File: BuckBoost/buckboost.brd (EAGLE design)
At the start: 100 x 80 mm, 8 parts

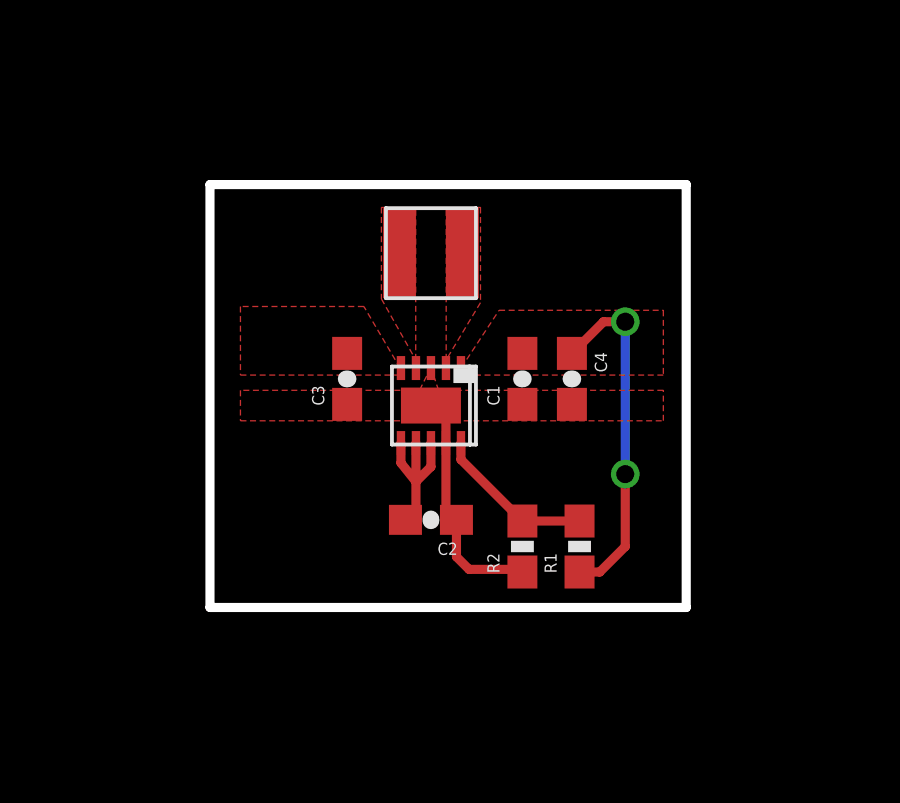
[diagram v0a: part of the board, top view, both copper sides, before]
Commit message: Changed Resistor and Capacity sizes
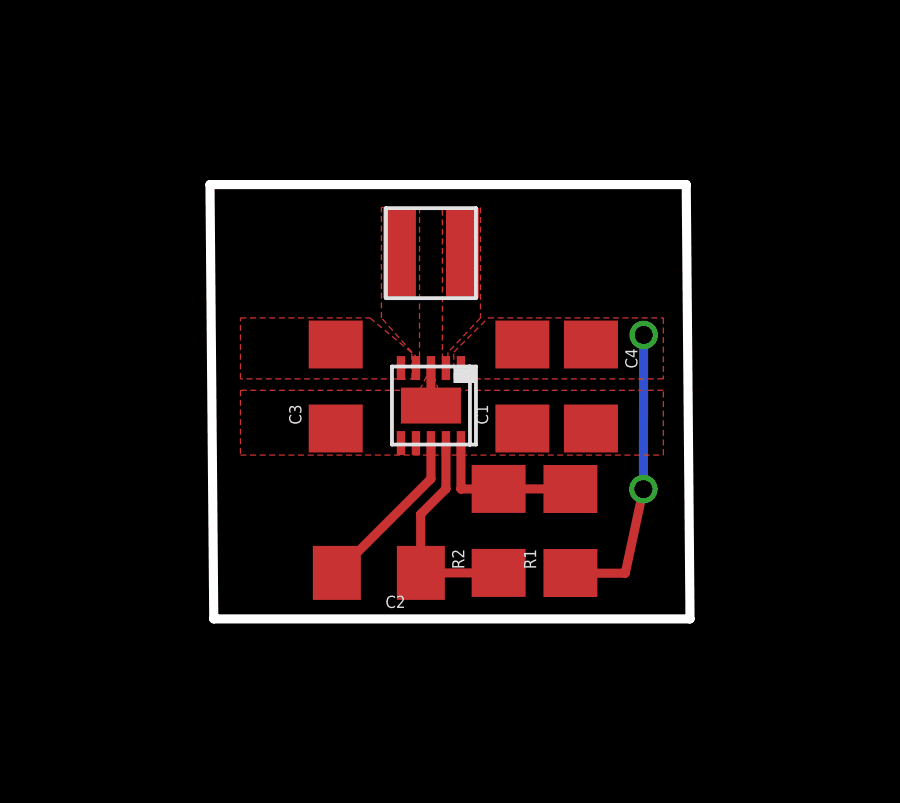
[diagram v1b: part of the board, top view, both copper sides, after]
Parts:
- C1, C2, C3, C4: device SparkFun-Passives:0603-CAP -> SparkFun-Capacitors:1206
- R1, R2: device SparkFun-Resistors:0603-RES -> SparkFun-Resistors:1206
- moved C2 2.48 mm to (13.5, 12.2)
- moved R2 0.95 mm to (17.5, 13.6)
- moved C4 0.68 mm to (20.6, 18.4)
- moved R1 0.60 mm to (19.9, 13.6)
- moved C3 0.46 mm to (12.1, 18.4)
- moved C1 0.25 mm to (18.3, 18.4)
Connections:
- new net N$2: U$1.6
- net N$3: no longer U$1.6, U$1.7
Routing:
- net VOUT: track 11.6 -> 9.84 mm
- net GND: track 7.80 -> 8.53 mm
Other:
- outline, holes or cut-outs redrawn

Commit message: PCB finished, only need to fix labels
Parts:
- added J1: (no value), SparkFun-Connectors:1X04
- added J2: (no value), SparkFun-Connectors:1X05
- added SJ1, SJ2: SOLDERJUMPERNC, SparkFun-Retired:SJ_2S
- moved R2 0.18 mm to (17.6, 13.5)
- moved R1 0.18 mm to (20.0, 13.5)
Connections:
- new net N$4: SJ2.2, U$1.7
- net GND: now also J2.2, J2.3, SJ2.1
- net N$2: now also SJ1.2
- net VIN: now also J2.1, J2.4, J2.5, SJ1.1
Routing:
- net N$2: track 0.00 -> 11.3 mm, vias 0 -> 2
- net N$4: track 0.00 -> 5.16 mm
- net VOUT: track 9.84 -> 10.4 mm
- added copper zone on layer 16, net GND
- added copper zone on layer 16, net VIN
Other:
- board size 100 x 80 mm -> 100.1 x 80.4 mm

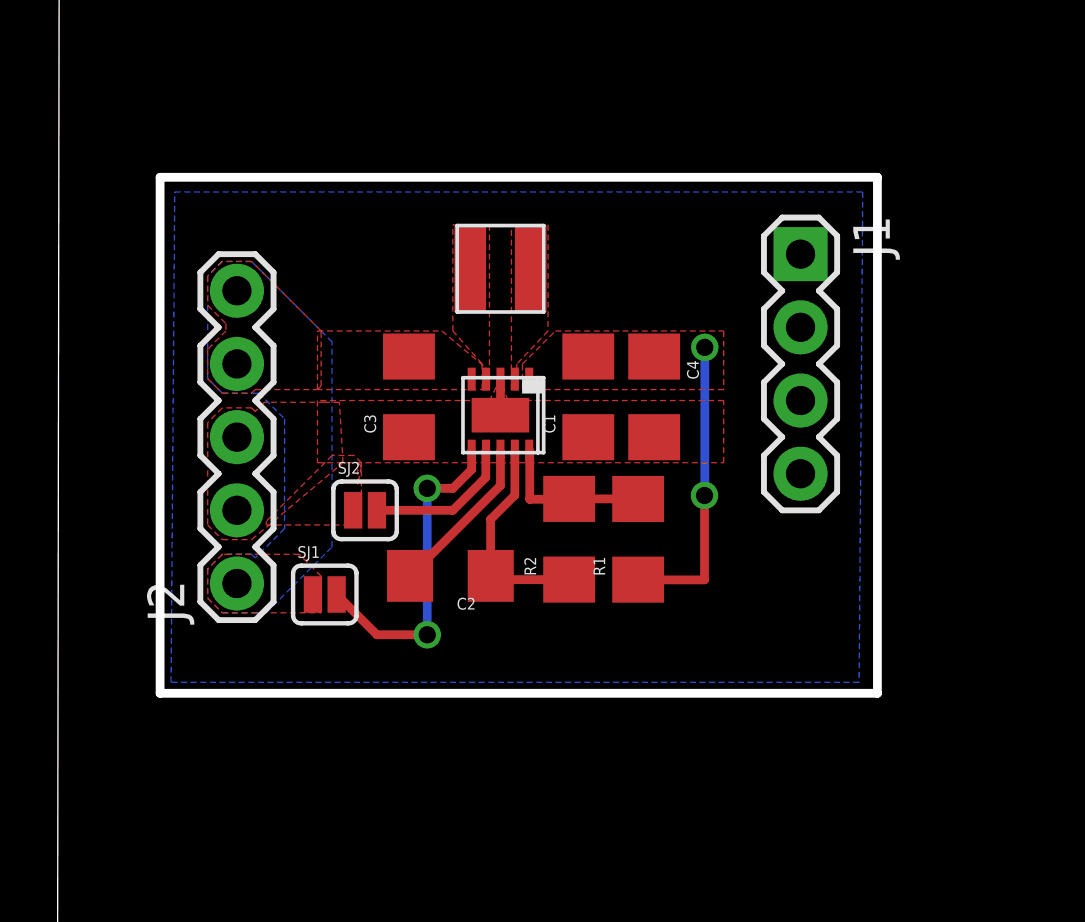
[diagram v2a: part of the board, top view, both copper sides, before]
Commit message: Headers Aligned for breadBoard
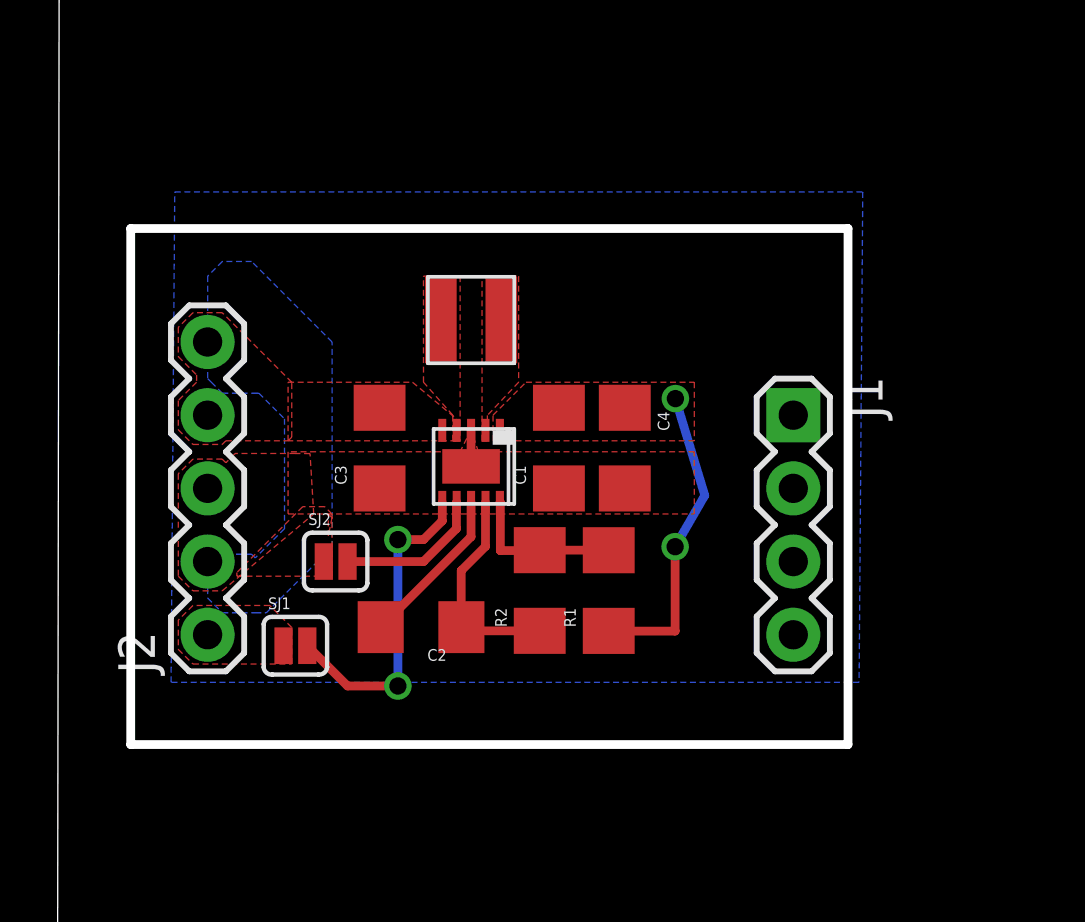
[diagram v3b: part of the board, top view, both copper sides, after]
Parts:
- moved J1 5.59 mm to (25.4, 17.8)
- moved U$1 2.05 mm to (14.2, 16.0)
- moved C2 2.05 mm to (12.5, 10.4)
- moved J2 2.05 mm to (5.08, 10.2)
- moved SJ1 2.05 mm to (8.12, 9.78)
- moved SJ2 2.05 mm to (9.52, 12.7)
- moved C1 2.05 mm to (17.3, 16.6)
- moved C3 2.05 mm to (11.0, 16.6)
- moved C4 2.05 mm to (19.6, 16.6)
- moved L1 2.05 mm to (14.2, 21.1)
- moved R1 2.05 mm to (19.0, 11.7)
- moved R2 2.05 mm to (16.6, 11.7)
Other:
- outline, holes or cut-outs redrawn

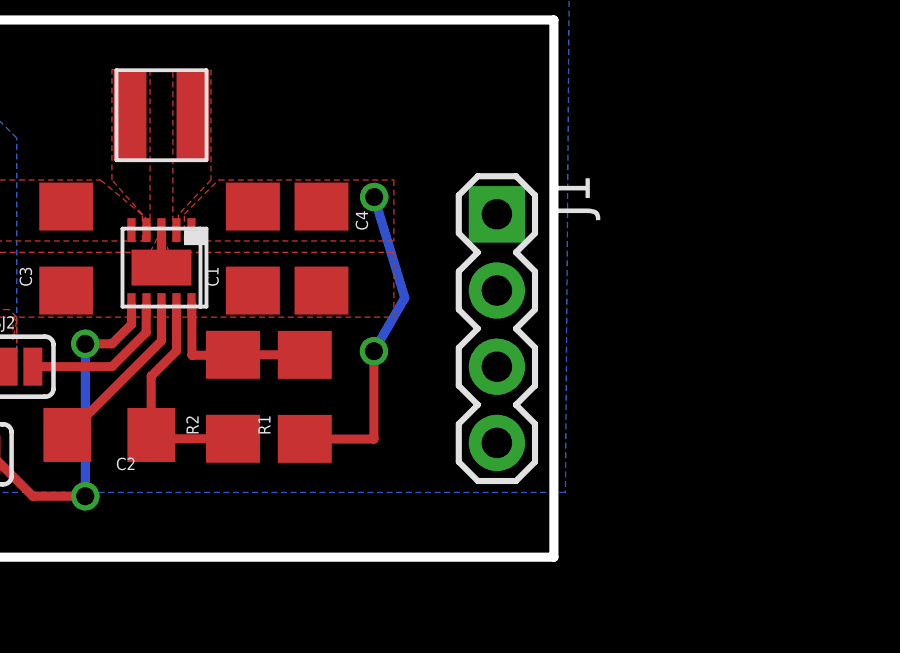
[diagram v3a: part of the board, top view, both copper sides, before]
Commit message: Finshed VOUT, just labels
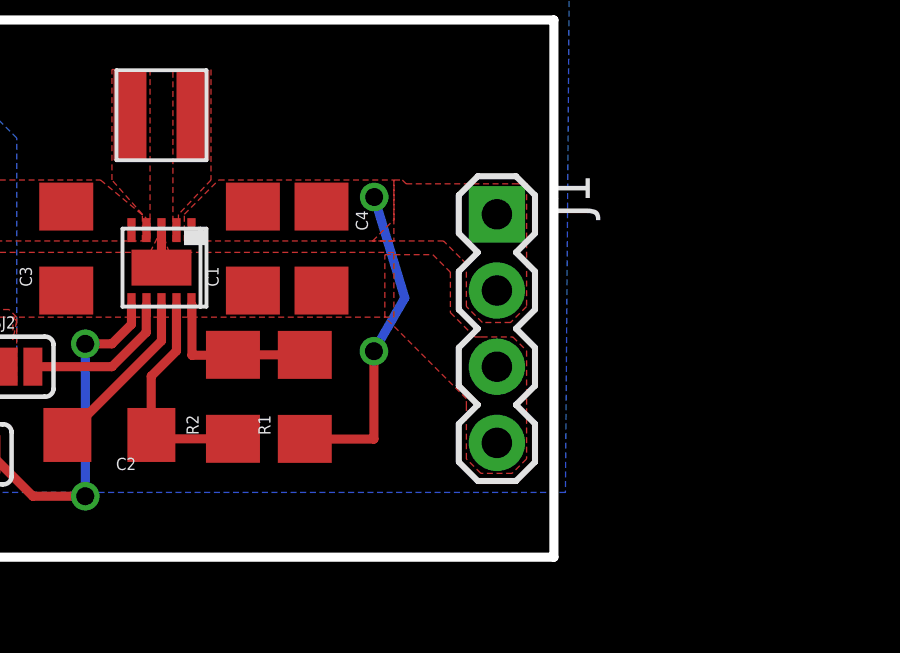
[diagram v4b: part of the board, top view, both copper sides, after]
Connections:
- net GND: now also J1.3, J1.4
- net VOUT: now also J1.1, J1.2
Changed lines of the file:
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@@
 <setting verticaltext="up"/>
 </settings>
-<grid distance="2.54" unitdist="mm" unit="mm" style="lines" multiple="1" display="yes" altdistance="0.000000123031" altunitdist="inch" altunit="inch"/>
+<grid distance="0.0254" unitdist="mm" unit="mm" style="lines" multiple="1" display="yes" altdistance="0.00254" altunitdist="mm" altunit="mm"/>
 <layers>
 <layer number="1" name="Top" color="4" fill="1" visible="yes" active="yes"/>
@@
 <wire x1="21.30178125" y1="13.21575" x2="22.3308" y2="14.99375" width="0.3048" layer="16"/>
 <wire x1="22.3308" y1="14.99375" x2="21.31115625" y2="18.354959375" width="0.3048" layer="16"/>
+<polygon width="0.3048" layer="1" thermals="no" rank="2">
+<vertex x="21.971" y="18.923"/>
+<vertex x="22.2504" y="18.923"/>
+<vertex x="22.3774" y="18.796"/>
+<vertex x="25.9588" y="18.796"/>
+<vertex x="26.416" y="18.796"/>
+<vertex x="26.3906" y="18.7706"/>
+<vertex x="26.3906" y="14.7066"/>
+<vertex x="25.8826" y="14.1986"/>
+<vertex x="25.8572" y="14.1732"/>
+<vertex x="24.9174" y="14.1732"/>
+<vertex x="24.384" y="14.7066"/>
+<vertex x="24.384" y="16.129"/>
+<vertex x="24.1808" y="16.3322"/>
+<vertex x="23.622" y="16.891"/>
+<vertex x="21.2598" y="16.891"/>
+<vertex x="21.971" y="17.6022"/>
+</polygon>
+<contactref element="J1" pad="1"/>
+<contactref element="J1" pad="2"/>
 </signal>
 <signal name="N$1">
@@
 <vertex x="9.39435625" y="14.224"/>
 </polygon>
+<contactref element="J1" pad="3"/>
+<contactref element="J1" pad="4"/>
+<polygon width="0.3048" layer="1" thermals="no" rank="2">
+<vertex x="24.892" y="13.6906"/>
+<vertex x="25.9334" y="13.6906"/>
+<vertex x="26.3906" y="13.2334"/>
+<vertex x="26.3906" y="9.6266"/>
+<vertex x="25.908" y="9.144"/>
+<vertex x="24.8666" y="9.144"/>
+<vertex x="24.384" y="9.6266"/>
+<vertex x="24.384" y="11.3538"/>
+<vertex x="24.384" y="11.6332"/>
+<vertex x="21.6662" y="14.351"/>
+<vertex x="21.6662" y="16.4338"/>
+<vertex x="23.2664" y="16.4338"/>
+<vertex x="23.8506" y="15.8496"/>
+<vertex x="23.8506" y="14.5034"/>
+<vertex x="24.6634" y="13.6906"/>
+<vertex x="24.8666" y="13.6906"/>
+</polygon>
 </signal>

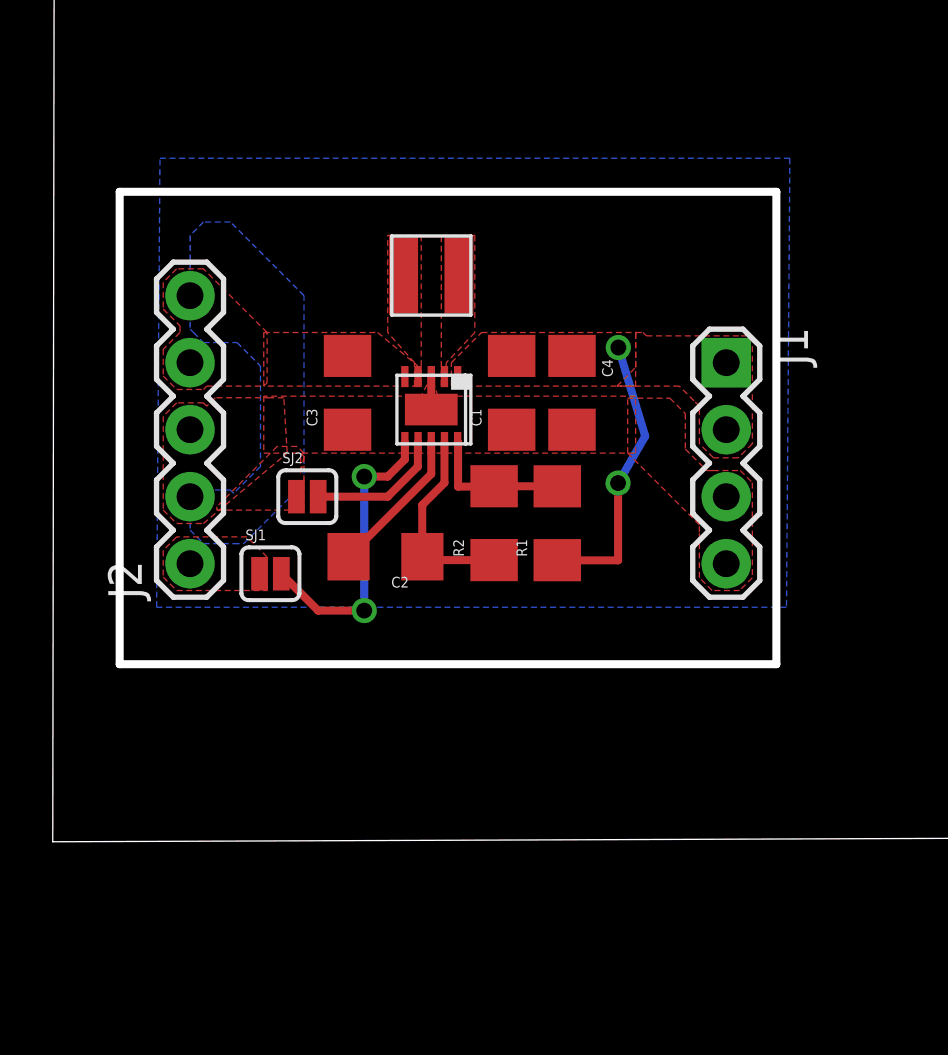
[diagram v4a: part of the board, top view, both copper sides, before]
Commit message: added 6 header
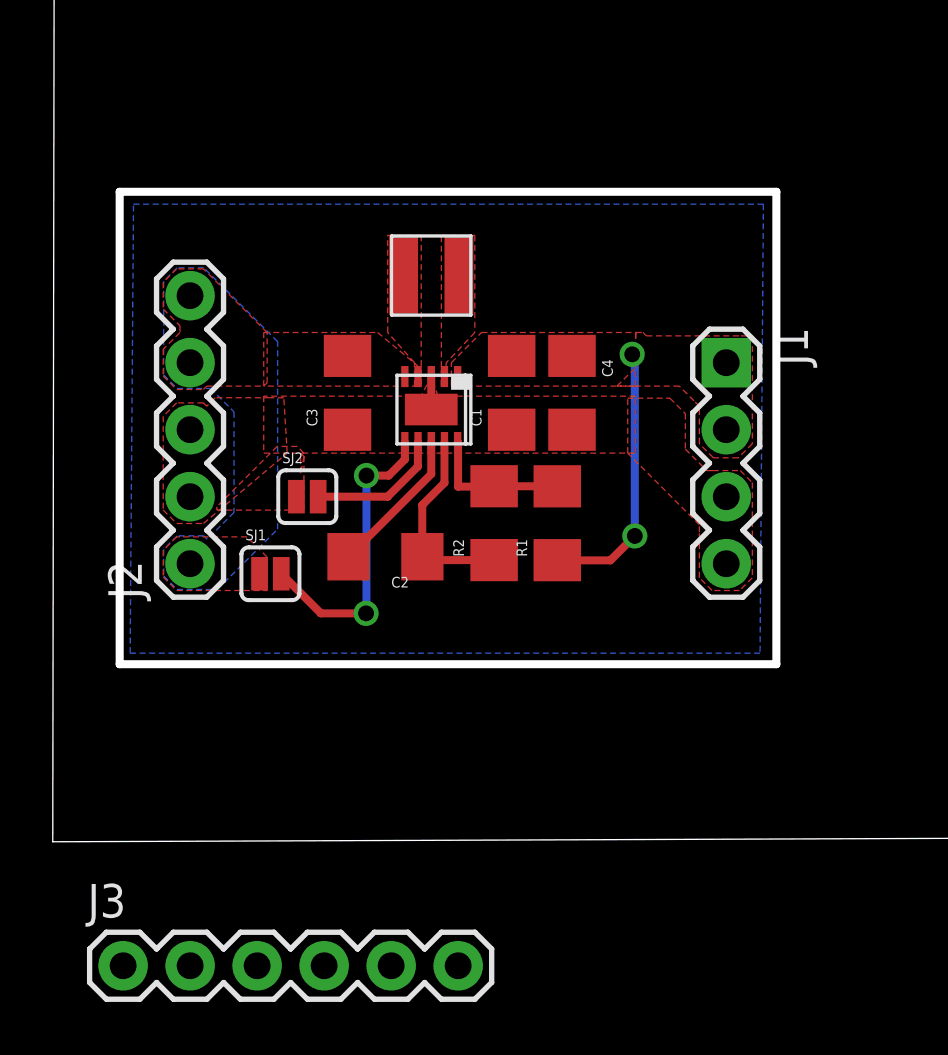
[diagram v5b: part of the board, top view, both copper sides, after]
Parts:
- added J3: (no value), SparkFun-Connectors:1X06
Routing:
- net VOUT: track 10.8 -> 10.3 mm
